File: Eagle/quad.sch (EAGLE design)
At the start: 12 parts

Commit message: Worked on board for the large quad.
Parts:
- removed AUX: (no value), con-lstb:MA06-1
- removed RECIEVER: (no value), con-lstb:MA10-1
- removed SV1: (no value), con-lstb:MA03-1
- added BACKLEFT, BACKRIGHT, FRONTLEFT, FRONTRIGHT: LSP11, solpad:LSP11
- added MODUL2: ARDUINO_NANO2, arduino:ARDUINO_NANO2
- added PROXSENS: (no value), con-lstb:MA06-1
- added RADIO: (no value), con-lstb:MA08-1
- added USBACK, USFRONT, USLEFT, USRIGHT: (no value), con-lstb:MA04-1
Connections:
- new net N$22: MODUL2.D4, USFRONT.2
- new net N$23: MODUL2.D5, USFRONT.3
- new net N$24: MODUL2.D2, USLEFT.2
- new net N$25: MODUL2.D3, USLEFT.3
- new net N$26: MODUL2.D6, USRIGHT.2
- new net N$27: MODUL2.D7, USRIGHT.3
- new net N$29: MODUL2.D9, USBACK.3
- new net N$30: MODUL2.D8, USBACK.2
- net N$1: now also FRONTLEFT.MP; no longer RECIEVER.1
- net N$10: now also MODUL2.A1, PROXSENS.5; no longer AUX.6, MODUL1.A0
- net N$11: now also RADIO.4; no longer RECIEVER.5
- net N$12: now also RADIO.5; no longer RECIEVER.6
- net N$13: now also RADIO.6; no longer RECIEVER.7
- net N$14: now also MODUL2.3V3
- net N$15: now also MODUL2.A7; no longer MODUL1.A7
- net N$16: now also MODUL2.A5
- net N$17: now also MODUL2.A4
- net N$18: now also MODUL2.A6; no longer MODUL1.A6
- net N$19: now also MODUL2.A0, PROXSENS.6; no longer AUX.5, MODUL1.A1
- net N$2: now also MODUL2.+5V, PROXSENS.1, PROXSENS.2, RADIO.7, USBACK.1, USFRONT.1, USLEFT.1, USRIGHT.1; no longer AUX.3, AUX.4, RECIEVER.8
- net N$3: now also BACKLEFT.MP; no longer SV1.3
- net N$4: now also BACKRIGHT.MP; no longer SV1.1
- net N$5: now also RADIO.1; no longer RECIEVER.2
- net N$6: now also FRONTRIGHT.MP; no longer RECIEVER.10
- net N$7: now also RADIO.2; no longer RECIEVER.3
- net N$8: now also RADIO.3; no longer RECIEVER.4
- net N$9: now also MODUL2.COM, MODUL2.COM@1, PROXSENS.3, PROXSENS.4, RADIO.8, USBACK.4, USFRONT.4, USLEFT.4, USRIGHT.4; no longer AUX.1, AUX.2, RECIEVER.9

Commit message: Simplified large board. Planning to put distance sensors on a separate board.
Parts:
- removed PROXSENS: (no value), con-lstb:MA06-1
- removed USBACK, USFRONT, USLEFT, USRIGHT: (no value), con-lstb:MA04-1
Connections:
- removed net N$10: MODUL2.A1, PROXSENS.5
- removed net N$19: MODUL2.A0, PROXSENS.6
- removed net N$22: MODUL2.D4, USFRONT.2
- removed net N$23: MODUL2.D5, USFRONT.3
- removed net N$24: MODUL2.D2, USLEFT.2
- removed net N$25: MODUL2.D3, USLEFT.3
- removed net N$26: MODUL2.D6, USRIGHT.2
- removed net N$27: MODUL2.D7, USRIGHT.3
- removed net N$29: MODUL2.D9, USBACK.3
- removed net N$30: MODUL2.D8, USBACK.2
- net N$2: no longer PROXSENS.1, PROXSENS.2, USBACK.1, USFRONT.1, USLEFT.1, USRIGHT.1
- net N$9: no longer PROXSENS.3, PROXSENS.4, USBACK.4, USFRONT.4, USLEFT.4, USRIGHT.4

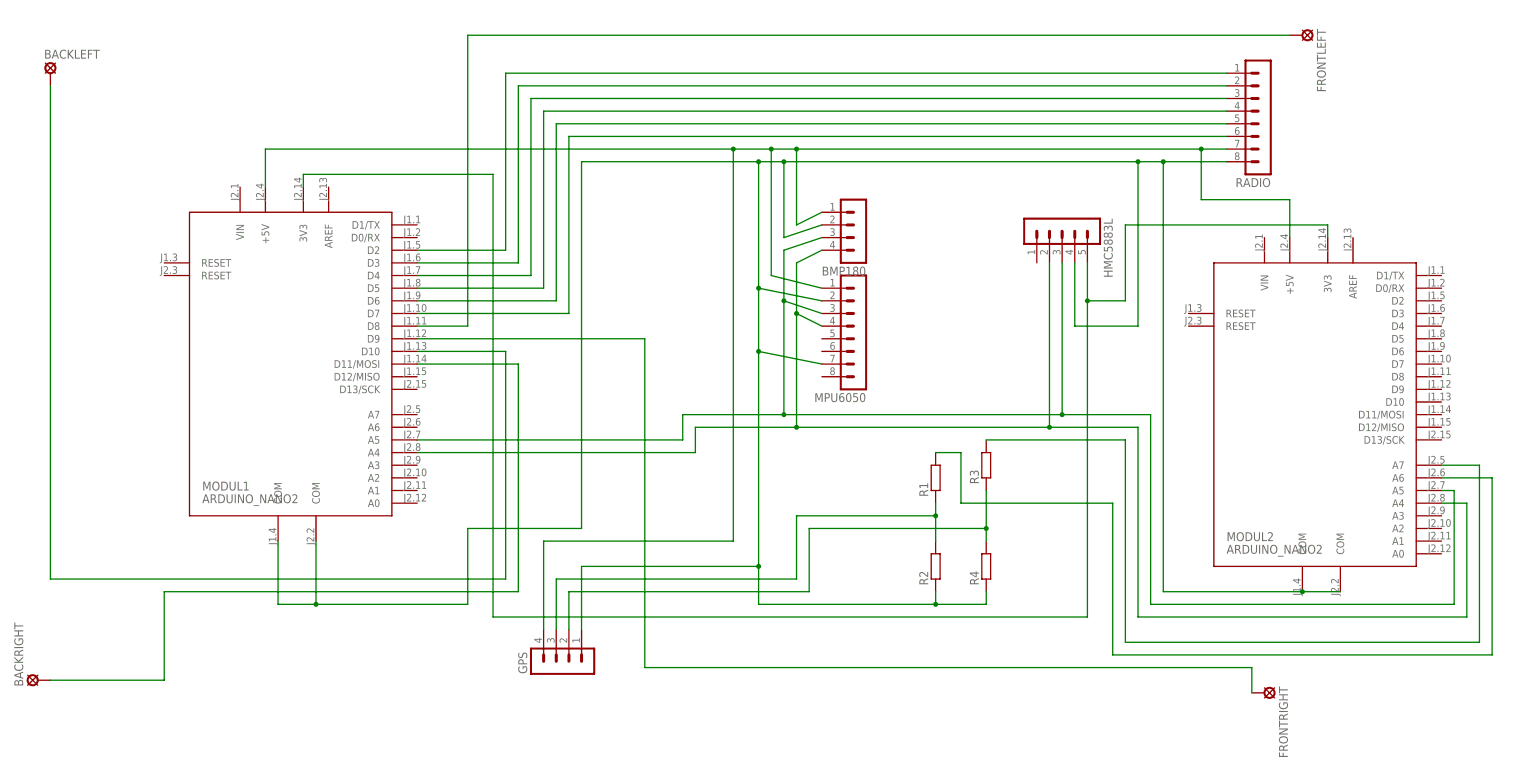
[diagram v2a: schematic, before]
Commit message: Fixed trace width.
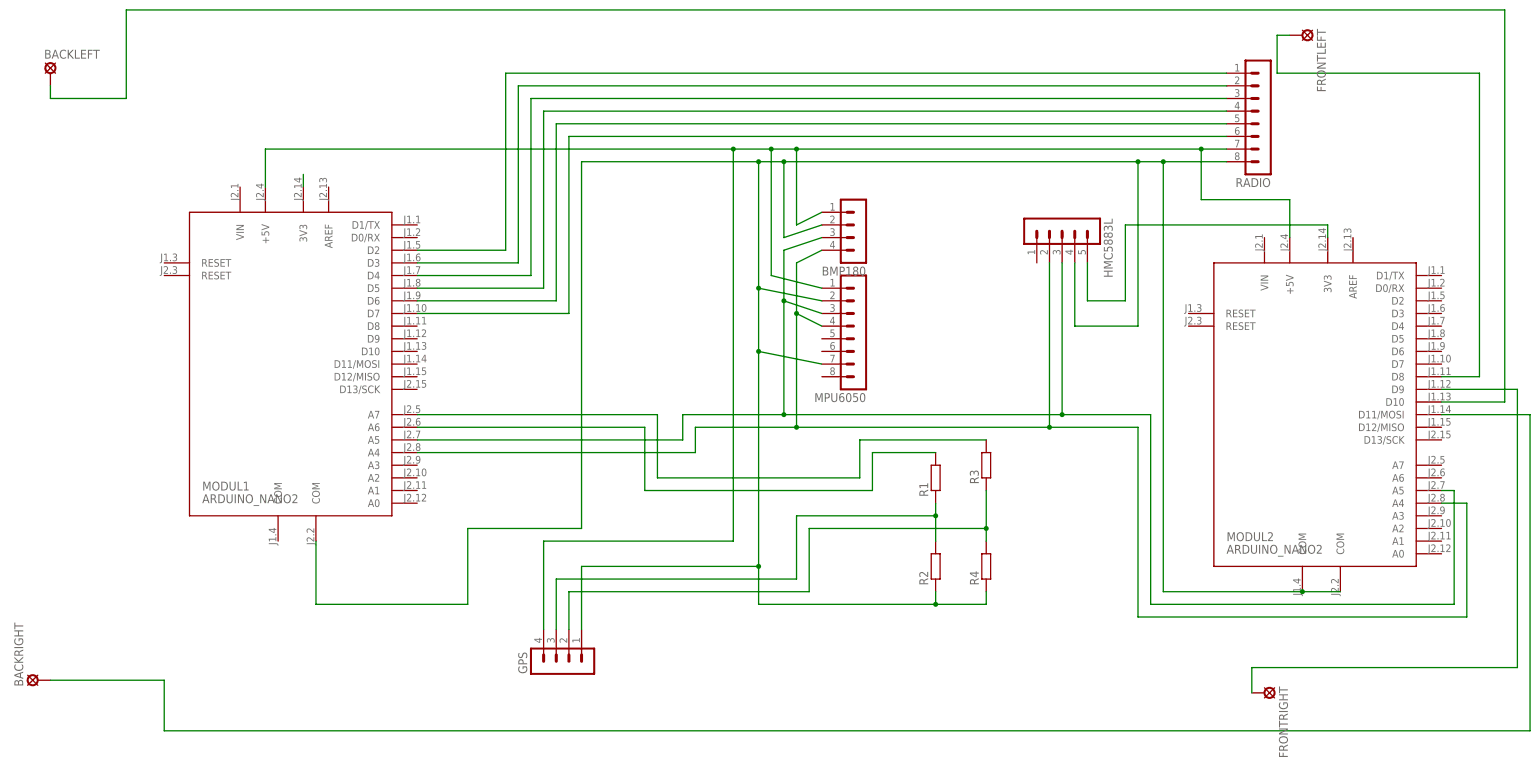
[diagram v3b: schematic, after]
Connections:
- new net N$10: MODUL1.A6, R1.2
- net N$1: now also MODUL2.D8; no longer MODUL1.D8
- net N$14: no longer MODUL1.3V3
- net N$15: now also MODUL1.3V3; no longer MODUL2.A7, R3.2
- net N$18: now also MODUL1.A7, R3.2; no longer MODUL2.A6, R1.2
- net N$3: now also MODUL2.D10; no longer MODUL1.D10
- net N$4: now also MODUL2.D11/MOSI; no longer MODUL1.D11/MOSI
- net N$6: now also MODUL2.D9; no longer MODUL1.D9
- net N$9: no longer MODUL1.COM
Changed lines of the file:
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@@
 <net name="N$1" class="0">
 <segment>
-<pinref part="MODUL1" gate="MODUL" pin="D8"/>
-<wire x1="35.56" y1="53.34" x2="45.72" y2="53.34" width="0.1524" layer="91"/>
-<wire x1="45.72" y1="53.34" x2="45.72" y2="111.76" width="0.1524" layer="91"/>
 <pinref part="FRONTLEFT" gate="1" pin="MP"/>
-<wire x1="45.72" y1="111.76" x2="210.82" y2="111.76" width="0.1524" layer="91"/>
+<pinref part="MODUL2" gate="MODUL" pin="D8"/>
+<wire x1="208.28" y1="111.76" x2="210.82" y2="111.76" width="0.1524" layer="91"/>
+<wire x1="241.3" y1="43.18" x2="248.92" y2="43.18" width="0.1524" layer="91"/>
+<wire x1="248.92" y1="43.18" x2="248.92" y2="104.14" width="0.1524" layer="91"/>
+<wire x1="248.92" y1="104.14" x2="208.28" y2="104.14" width="0.1524" layer="91"/>
+<wire x1="208.28" y1="104.14" x2="208.28" y2="111.76" width="0.1524" layer="91"/>
 </segment>
 </net>
 <net name="N$3" class="0">
 <segment>
-<pinref part="MODUL1" gate="MODUL" pin="D10"/>
-<wire x1="35.56" y1="48.26" x2="53.34" y2="48.26" width="0.1524" layer="91"/>
-<wire x1="-38.1" y1="2.54" x2="53.34" y2="2.54" width="0.1524" layer="91"/>
-<wire x1="53.34" y1="2.54" x2="53.34" y2="48.26" width="0.1524" layer="91"/>
 <pinref part="BACKLEFT" gate="1" pin="MP"/>
-<wire x1="-38.1" y1="2.54" x2="-38.1" y2="101.6" width="0.1524" layer="91"/>
+<pinref part="MODUL2" gate="MODUL" pin="D10"/>
+<wire x1="-38.1" y1="99.06" x2="-38.1" y2="101.6" width="0.1524" layer="91"/>
+<wire x1="241.3" y1="38.1" x2="254" y2="38.1" width="0.1524" layer="91"/>
+<wire x1="254" y1="38.1" x2="254" y2="116.84" width="0.1524" layer="91"/>
+<wire x1="254" y1="116.84" x2="-22.86" y2="116.84" width="0.1524" layer="91"/>
+<wire x1="-22.86" y1="116.84" x2="-22.86" y2="99.06" width="0.1524" layer="91"/>
+<wire x1="-22.86" y1="99.06" x2="-38.1" y2="99.06" width="0.1524" layer="91"/>
 </segment>
 </net>
@@
 <net name="N$6" class="0">
 <segment>
-<pinref part="MODUL1" gate="MODUL" pin="D9"/>
-<wire x1="35.56" y1="50.8" x2="81.28" y2="50.8" width="0.1524" layer="91"/>
-<wire x1="81.28" y1="50.8" x2="81.28" y2="-15.24" width="0.1524" layer="91"/>
 <pinref part="FRONTRIGHT" gate="1" pin="MP"/>
-<wire x1="81.28" y1="-15.24" x2="203.2" y2="-15.24" width="0.1524" layer="91"/>
 <wire x1="203.2" y1="-15.24" x2="203.2" y2="-20.32" width="0.1524" layer="91"/>
+<pinref part="MODUL2" gate="MODUL" pin="D9"/>
+<wire x1="241.3" y1="40.64" x2="256.54" y2="40.64" width="0.1524" layer="91"/>
+<wire x1="256.54" y1="40.64" x2="256.54" y2="-15.24" width="0.1524" layer="91"/>
+<wire x1="256.54" y1="-15.24" x2="203.2" y2="-15.24" width="0.1524" layer="91"/>
 </segment>
 </net>
@@
 <pinref part="R2" gate="G$1" pin="1"/>
 <wire x1="139.7" y1="0" x2="139.7" y2="-2.54" width="0.1524" layer="91"/>
-<pinref part="MODUL1" gate="MODUL" pin="COM"/>
-<wire x1="7.62" y1="10.16" x2="7.62" y2="-2.54" width="0.1524" layer="91"/>
-<wire x1="7.62" y1="-2.54" x2="15.24" y2="-2.54" width="0.1524" layer="91"/>
 <wire x1="15.24" y1="-2.54" x2="45.72" y2="-2.54" width="0.1524" layer="91"/>
 <wire x1="45.72" y1="-2.54" x2="45.72" y2="12.7" width="0.1524" layer="91"/>
 <wire x1="45.72" y1="12.7" x2="68.58" y2="12.7" width="0.1524" layer="91"/>
 <pinref part="MODUL1" gate="MODUL" pin="COM@1"/>
-<junction x="15.24" y="-2.54"/>
 <wire x1="15.24" y1="-2.54" x2="15.24" y2="10.16" width="0.1524" layer="91"/>
 <pinref part="RADIO" gate="1" pin="8"/>
@@
 <segment>
 <wire x1="170.18" y1="66.04" x2="170.18" y2="58.42" width="0.1524" layer="91"/>
-<wire x1="170.18" y1="58.42" x2="170.18" y2="-5.08" width="0.1524" layer="91"/>
-<wire x1="170.18" y1="-5.08" x2="50.8" y2="-5.08" width="0.1524" layer="91"/>
-<wire x1="50.8" y1="83.82" x2="50.8" y2="-5.08" width="0.1524" layer="91"/>
-<wire x1="50.8" y1="83.82" x2="12.7" y2="83.82" width="0.1524" layer="91"/>
-<pinref part="MODUL1" gate="MODUL" pin="3V3"/>
-<wire x1="12.7" y1="83.82" x2="12.7" y2="81.28" width="0.1524" layer="91"/>
 <pinref part="HMC5883L" gate="G$1" pin="5"/>
 <pinref part="MODUL2" gate="MODUL" pin="3V3"/>
@@
 <wire x1="177.8" y1="73.66" x2="177.8" y2="58.42" width="0.1524" layer="91"/>
 <wire x1="177.8" y1="58.42" x2="170.18" y2="58.42" width="0.1524" layer="91"/>
-<junction x="170.18" y="58.42"/>
-</segment>
-</net>
-<net name="N$15" class="0">
-<segment>
-<pinref part="R3" gate="G$1" pin="2"/>
-<wire x1="149.86" y1="30.48" x2="177.8" y2="30.48" width="0.1524" layer="91"/>
-<wire x1="177.8" y1="30.48" x2="177.8" y2="-10.16" width="0.1524" layer="91"/>
-<wire x1="177.8" y1="-10.16" x2="248.92" y2="-10.16" width="0.1524" layer="91"/>
-<wire x1="248.92" y1="-10.16" x2="248.92" y2="25.4" width="0.1524" layer="91"/>
-<pinref part="MODUL2" gate="MODUL" pin="A7"/>
-<wire x1="248.92" y1="25.4" x2="241.3" y2="25.4" width="0.1524" layer="91"/>
-</segment>
-</net>
-<net name="N$18" class="0">
-<segment>
-<pinref part="R1" gate="G$1" pin="2"/>
-<pinref part="MODUL2" gate="MODUL" pin="A6"/>
-<wire x1="241.3" y1="22.86" x2="251.46" y2="22.86" width="0.1524" layer="91"/>
-<wire x1="251.46" y1="22.86" x2="251.46" y2="-12.7" width="0.1524" layer="91"/>
-<wire x1="251.46" y1="-12.7" x2="175.26" y2="-12.7" width="0.1524" layer="91"/>
-<wire x1="175.26" y1="-12.7" x2="175.26" y2="17.78" width="0.1524" layer="91"/>
-<wire x1="175.26" y1="17.78" x2="144.78" y2="17.78" width="0.1524" layer="91"/>
-<wire x1="144.78" y1="17.78" x2="144.78" y2="27.94" width="0.1524" layer="91"/>
-<wire x1="144.78" y1="27.94" x2="139.7" y2="27.94" width="0.1524" layer="91"/>
 </segment>
 </net>
@@
 <net name="N$4" class="0">
 <segment>
-<pinref part="MODUL1" gate="MODUL" pin="D11/MOSI"/>
-<wire x1="35.56" y1="45.72" x2="55.88" y2="45.72" width="0.1524" layer="91"/>
-<wire x1="55.88" y1="45.72" x2="55.88" y2="0" width="0.1524" layer="91"/>
-<wire x1="55.88" y1="0" x2="-15.24" y2="0" width="0.1524" layer="91"/>
 <pinref part="BACKRIGHT" gate="1" pin="MP"/>
 <wire x1="-38.1" y1="-17.78" x2="-15.24" y2="-17.78" width="0.1524" layer="91"/>
-<wire x1="-15.24" y1="-17.78" x2="-15.24" y2="0" width="0.1524" layer="91"/>
-</segment>
-</net>
+<pinref part="MODUL2" gate="MODUL" pin="D11/MOSI"/>
+<wire x1="241.3" y1="35.56" x2="259.08" y2="35.56" width="0.1524" layer="91"/>
+<wire x1="259.08" y1="35.56" x2="259.08" y2="-27.94" width="0.1524" layer="91"/>
+<wire x1="259.08" y1="-27.94" x2="-15.24" y2="-27.94" width="0.1524" layer="91"/>
+<wire x1="-15.24" y1="-27.94" x2="-15.24" y2="-17.78" width="0.1524" layer="91"/>
+</segment>
+</net>
+<net name="N$10" class="0">
+<segment>
+<pinref part="R1" gate="G$1" pin="2"/>
+<wire x1="127" y1="27.94" x2="139.7" y2="27.94" width="0.1524" layer="91"/>
+<wire x1="127" y1="20.32" x2="127" y2="27.94" width="0.1524" layer="91"/>
+<wire x1="81.28" y1="20.32" x2="127" y2="20.32" width="0.1524" layer="91"/>
+<wire x1="81.28" y1="33.02" x2="81.28" y2="20.32" width="0.1524" layer="91"/>
+<pinref part="MODUL1" gate="MODUL" pin="A6"/>
+<wire x1="35.56" y1="33.02" x2="81.28" y2="33.02" width="0.1524" layer="91"/>
+</segment>
+</net>
+<net name="N$18" class="0">
+<segment>
+<pinref part="R3" gate="G$1" pin="2"/>
+<wire x1="124.46" y1="30.48" x2="149.86" y2="30.48" width="0.1524" layer="91"/>
+<wire x1="124.46" y1="22.86" x2="124.46" y2="30.48" width="0.1524" layer="91"/>
+<wire x1="83.82" y1="22.86" x2="124.46" y2="22.86" width="0.1524" layer="91"/>
+<wire x1="83.82" y1="35.56" x2="83.82" y2="22.86" width="0.1524" layer="91"/>
+<pinref part="MODUL1" gate="MODUL" pin="A7"/>
+<wire x1="35.56" y1="35.56" x2="83.82" y2="35.56" width="0.1524" layer="91"/>
+</segment>
+</net>
+<net name="N$15" class="0">
+<segment>
+<pinref part="MODUL1" gate="MODUL" pin="3V3"/>
+<wire x1="12.7" y1="83.82" x2="12.7" y2="81.28" width="0.1524" layer="91"/>
+</segment>
+</net>

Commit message: Final board design and added ground fill.
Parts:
- removed BMP180: (no value), con-lstb:MA04-1
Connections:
- removed net N$2: BMP180.1, GPS.4, MODUL1.+5V, MODUL2.+5V, MPU6050.1, RADIO.7
- removed net N$9: BMP180.2, GPS.1, HMC5883L.4, MODUL1.COM@1, MODUL2.COM, MODUL2.COM@1, MPU6050.2, MPU6050.7, R2.1, R4.1, RADIO.8
- new net GND: GPS.1, HMC5883L.4, MODUL1.COM, MODUL1.COM@1, MODUL2.COM, MODUL2.COM@1, MPU6050.2, MPU6050.7, R2.1, R4.1, RADIO.8
- new net VDD: GPS.4, MODUL1.+5V, MODUL2.+5V, MPU6050.1, RADIO.7
- net N$16: no longer BMP180.3
- net N$17: no longer BMP180.4
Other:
- moved on the sheet: MPU6050
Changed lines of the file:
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@@
 <part name="MODUL1" library="arduino" deviceset="ARDUINO_NANO2" device=""/>
 <part name="MPU6050" library="con-lstb" deviceset="MA08-1" device=""/>
-<part name="BMP180" library="con-lstb" deviceset="MA04-1" device=""/>
 <part name="R1" library="rcl" deviceset="R-EU_" device="0207/10"/>
 <part name="R2" library="rcl" deviceset="R-EU_" device="0207/10"/>
@@
 <instances>
 <instance part="MODUL1" gate="MODUL" x="10.16" y="45.72"/>
-<instance part="MPU6050" gate="1" x="124.46" y="53.34" rot="R180"/>
-<instance part="BMP180" gate="1" x="124.46" y="71.12" rot="R180"/>
+<instance part="MPU6050" gate="1" x="124.46" y="55.88" rot="R180"/>
 <instance part="R1" gate="G$1" x="139.7" y="22.86" rot="R90"/>
 <instance part="R2" gate="G$1" x="139.7" y="5.08" rot="R90"/>
@@
 </segment>
 </net>
-<net name="N$2" class="0">
+<net name="VDD" class="0">
 <segment>
 <wire x1="198.12" y1="88.9" x2="193.04" y2="88.9" width="0.1524" layer="91"/>
-<wire x1="193.04" y1="88.9" x2="111.76" y2="88.9" width="0.1524" layer="91"/>
-<wire x1="111.76" y1="88.9" x2="106.68" y2="88.9" width="0.1524" layer="91"/>
+<wire x1="193.04" y1="88.9" x2="106.68" y2="88.9" width="0.1524" layer="91"/>
 <wire x1="106.68" y1="88.9" x2="99.06" y2="88.9" width="0.1524" layer="91"/>
 <wire x1="99.06" y1="88.9" x2="5.08" y2="88.9" width="0.1524" layer="91"/>
-<wire x1="111.76" y1="73.66" x2="111.76" y2="88.9" width="0.1524" layer="91"/>
-<junction x="111.76" y="88.9"/>
 <junction x="106.68" y="88.9"/>
 <wire x1="106.68" y1="88.9" x2="106.68" y2="63.5" width="0.1524" layer="91"/>
@@
 <pinref part="MODUL1" gate="MODUL" pin="+5V"/>
 <wire x1="5.08" y1="81.28" x2="5.08" y2="88.9" width="0.1524" layer="91"/>
-<pinref part="BMP180" gate="1" pin="1"/>
-<wire x1="111.76" y1="73.66" x2="116.84" y2="76.2" width="0.1524" layer="91"/>
 <pinref part="MPU6050" gate="1" pin="1"/>
-<wire x1="106.68" y1="63.5" x2="116.84" y2="60.96" width="0.1524" layer="91"/>
+<wire x1="106.68" y1="63.5" x2="116.84" y2="63.5" width="0.1524" layer="91"/>
 <pinref part="GPS" gate="1" pin="4"/>
 <pinref part="RADIO" gate="1" pin="7"/>
@@
 </segment>
 </net>
-<net name="N$9" class="0">
+<net name="GND" class="0">
 <segment>
 <wire x1="198.12" y1="86.36" x2="185.42" y2="86.36" width="0.1524" layer="91"/>
 <wire x1="185.42" y1="86.36" x2="180.34" y2="86.36" width="0.1524" layer="91"/>
-<wire x1="180.34" y1="86.36" x2="109.22" y2="86.36" width="0.1524" layer="91"/>
-<wire x1="109.22" y1="86.36" x2="104.14" y2="86.36" width="0.1524" layer="91"/>
+<wire x1="180.34" y1="86.36" x2="104.14" y2="86.36" width="0.1524" layer="91"/>
 <wire x1="104.14" y1="86.36" x2="68.58" y2="86.36" width="0.1524" layer="91"/>
 <wire x1="68.58" y1="86.36" x2="68.58" y2="12.7" width="0.1524" layer="91"/>
-<wire x1="116.84" y1="73.66" x2="109.22" y2="71.12" width="0.1524" layer="91"/>
-<wire x1="109.22" y1="71.12" x2="109.22" y2="86.36" width="0.1524" layer="91"/>
-<junction x="109.22" y="86.36"/>
 <junction x="104.14" y="86.36"/>
 <wire x1="104.14" y1="86.36" x2="104.14" y2="60.96" width="0.1524" layer="91"/>
@@
 <junction x="104.14" y="48.26"/>
 <wire x1="104.14" y1="5.08" x2="104.14" y2="48.26" width="0.1524" layer="91"/>
-<pinref part="BMP180" gate="1" pin="2"/>
 <pinref part="MPU6050" gate="1" pin="2"/>
-<wire x1="116.84" y1="58.42" x2="104.14" y2="60.96" width="0.1524" layer="91"/>
+<wire x1="116.84" y1="60.96" x2="104.14" y2="60.96" width="0.1524" layer="91"/>
 <pinref part="MPU6050" gate="1" pin="7"/>
-<wire x1="104.14" y1="48.26" x2="116.84" y2="45.72" width="0.1524" layer="91"/>
+<wire x1="104.14" y1="48.26" x2="116.84" y2="48.26" width="0.1524" layer="91"/>
 <pinref part="HMC5883L" gate="G$1" pin="4"/>
 <pinref part="GPS" gate="1" pin="1"/>
@@
 <junction x="185.42" y="86.36"/>
 <junction x="213.36" y="0"/>
+<pinref part="MODUL1" gate="MODUL" pin="COM"/>
+<wire x1="7.62" y1="10.16" x2="7.62" y2="-2.54" width="0.1524" layer="91"/>
+<wire x1="7.62" y1="-2.54" x2="15.24" y2="-2.54" width="0.1524" layer="91"/>
+<junction x="15.24" y="-2.54"/>
 </segment>
 </net>
 <net name="N$16" class="0">
 <segment>
-<wire x1="116.84" y1="71.12" x2="109.22" y2="68.58" width="0.1524" layer="91"/>
-<wire x1="109.22" y1="68.58" x2="109.22" y2="58.42" width="0.1524" layer="91"/>
 <wire x1="109.22" y1="58.42" x2="109.22" y2="35.56" width="0.1524" layer="91"/>
-<junction x="109.22" y="58.42"/>
 <wire x1="109.22" y1="35.56" x2="165.1" y2="35.56" width="0.1524" layer="91"/>
 <wire x1="165.1" y1="35.56" x2="165.1" y2="66.04" width="0.1524" layer="91"/>
-<pinref part="BMP180" gate="1" pin="3"/>
 <pinref part="MPU6050" gate="1" pin="3"/>
-<wire x1="109.22" y1="58.42" x2="116.84" y2="55.88" width="0.1524" layer="91"/>
+<wire x1="109.22" y1="58.42" x2="116.84" y2="58.42" width="0.1524" layer="91"/>
 <pinref part="MODUL1" gate="MODUL" pin="A5"/>
 <wire x1="35.56" y1="30.48" x2="88.9" y2="30.48" width="0.1524" layer="91"/>
@@
 <segment>
 <wire x1="111.76" y1="33.02" x2="111.76" y2="55.88" width="0.1524" layer="91"/>
-<wire x1="111.76" y1="55.88" x2="111.76" y2="66.04" width="0.1524" layer="91"/>
-<junction x="111.76" y="55.88"/>
 <wire x1="162.56" y1="66.04" x2="162.56" y2="33.02" width="0.1524" layer="91"/>
 <wire x1="162.56" y1="33.02" x2="111.76" y2="33.02" width="0.1524" layer="91"/>
-<pinref part="BMP180" gate="1" pin="4"/>
-<wire x1="111.76" y1="66.04" x2="116.84" y2="68.58" width="0.1524" layer="91"/>
 <pinref part="MPU6050" gate="1" pin="4"/>
-<wire x1="116.84" y1="53.34" x2="111.76" y2="55.88" width="0.1524" layer="91"/>
+<wire x1="116.84" y1="55.88" x2="111.76" y2="55.88" width="0.1524" layer="91"/>
 <pinref part="MODUL1" gate="MODUL" pin="A4"/>
 <wire x1="35.56" y1="27.94" x2="91.44" y2="27.94" width="0.1524" layer="91"/>
